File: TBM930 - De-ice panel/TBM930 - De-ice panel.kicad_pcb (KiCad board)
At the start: 2 copper layers, 190.5 x 101.6 mm, 51 parts, among them J1 SW_AIRFRAME_DE_ICE, J2 SW_ICE_LIGHT, J3 SW_PROP_DE_ICE, J4 SW_WIND_SHIELD, J5 SW_PITOT_L_HTR, J6 SW_PITOT_R_HTR, J7 SW_INERT_SEP, J8 Barrel_Jack, SW1 SW_Push, SW2 Mini toggle - SPDT, SW3 Mini toggle - SPDT, SW4 Mini toggle - SPDT, SW5 Mini toggle - SPDT, SW6 Mini toggle - SPDT, SW7 Mini toggle - SPDT, SW8 Mini toggle - SPDT, U1 Sparkfun_Pro_Micro, U2 TLC5917IN, U3 TLC5917IN

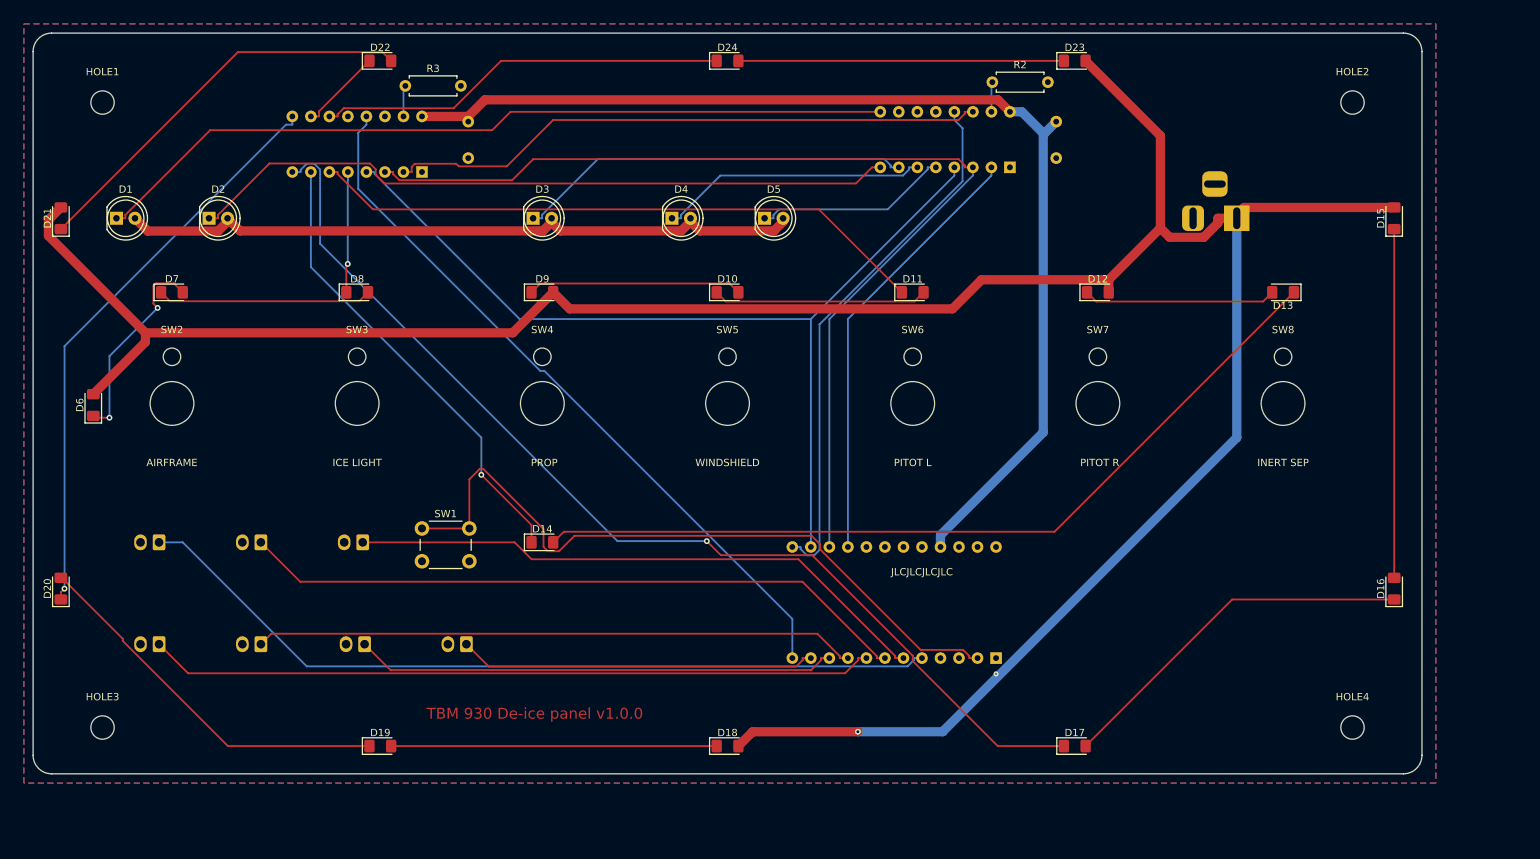
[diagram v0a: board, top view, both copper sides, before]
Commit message: Placed components on PCB, working on routing
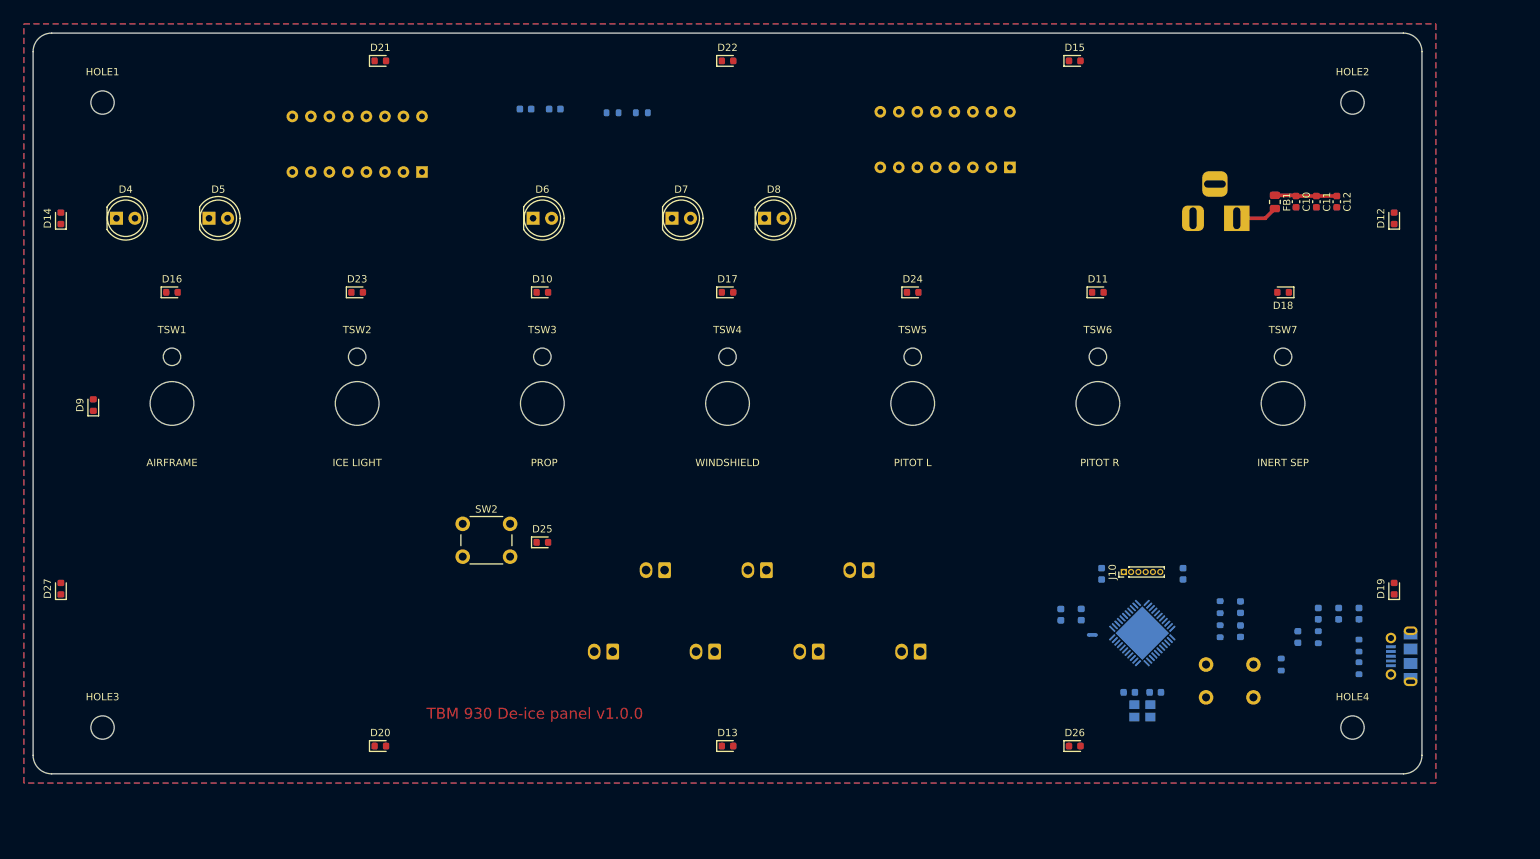
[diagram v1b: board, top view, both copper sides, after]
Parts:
- removed the J4 at (56.6, 126.4)
- removed the J5 at (70.6, 126.4)
- added C10: 10uF, Capacitor_SMD:C_0603_1608Metric, F.Cu at (212.6, 65.7)
- added C11: 1uF, Capacitor_SMD:C_0603_1608Metric, F.Cu at (215.4, 65.7)
- added C12: 0.1uF, Capacitor_SMD:C_0603_1608Metric, F.Cu at (218.2, 65.7)
- added C13: 0.1uF, Capacitor_SMD:C_0603_1608Metric, B.Cu at (106.9, 53.0)
- added C14: 0.1uF, Capacitor_SMD:C_0603_1608Metric, B.Cu at (110.9, 53.0)
- added C3: 20pF, Capacitor_SMD:C_0603_1608Metric, B.Cu at (189.7, 133.0)
- added C4: 20pF, Capacitor_SMD:C_0603_1608Metric, B.Cu at (193.3, 133.0)
- added C5: 10uF, Capacitor_SMD:C_0603_1608Metric, B.Cu at (221.2, 122.2)
- added C6: 1uF, Capacitor_SMD:C_0603_1608Metric, B.Cu at (218.4, 122.2)
- added C7: 0.1uF, Capacitor_SMD:C_0603_1608Metric, B.Cu at (215.6, 122.2)
- added C8: 1uF, Capacitor_SMD:C_0603_1608Metric, B.Cu at (183.1, 122.3)
- added C9: 0.1uF, Capacitor_SMD:C_0603_1608Metric, B.Cu at (180.3, 122.3)
- added D1: LED, LED_SMD:LED_0603_1608Metric, B.Cu at (212.9, 125.4)
- added D2: LED, LED_SMD:LED_0603_1608Metric, B.Cu at (205.0, 121.3)
- added D3: LED, LED_SMD:LED_0603_1608Metric, B.Cu at (205.0, 124.6)
- added FB1: Ferrite_Bead, Resistor_SMD:R_0805_2012Metric, F.Cu at (209.7, 65.7)
- added J1: USB_B_Micro, Connector_USB:USB_Micro-B_Molex-105017-0001, B.Cu at (227.1, 128.0)
- added J10: AVR-ISP-6, Connector_PinHeader_1.00mm:PinHeader_1x06_P1.00mm_Vertical, F.Cu at (189.0, 116.5)
- added J8: SW_PITOT_R_HTR, Connector_Molex:Molex_KK-254_AE-6410-02A_1x02_P2.54mm_Vertical, B.Cu at (147.1, 127.4)
- added J9: SW_INERT_SEP, Connector_Molex:Molex_KK-254_AE-6410-02A_1x02_P2.54mm_Vertical, B.Cu at (161.0, 127.4)
- added NT1: Net-Tie_2, NetTie:NetTie-2_SMD_Pad0.5mm, B.Cu at (184.7, 125.1)
- added R1: 10K, Resistor_SMD:R_0603_1608Metric, B.Cu at (210.6, 129.2)
- added R4: 1K, Resistor_SMD:R_0603_1608Metric, B.Cu at (215.6, 125.4)
- added R5: 330, Resistor_SMD:R_0603_1608Metric, B.Cu at (202.2, 121.3)
- added R6: 330, Resistor_SMD:R_0603_1608Metric, B.Cu at (202.2, 124.6)
- added R7: 1k, Resistor_SMD:R_0603_1608Metric, B.Cu at (118.9, 53.5)
- added R8: 1k, Resistor_SMD:R_0603_1608Metric, B.Cu at (122.9, 53.5)
- added SW2: SW_Push, Button_Switch_THT:SW_PUSH_6mm_H9.5mm, F.Cu at (98.3, 109.9)
- added Y1: 16MHz, Crystal:Crystal_SMD_3225-4Pin_3.2x2.5mm, B.Cu at (191.5, 135.5)
- C1, C2: value 0.1uF -> 1uF; footprint Capacitor_THT:C_Disc_D5.0mm_W2.5mm_P5.00mm -> Capacitor_SMD:C_0603_1608Metric
- D10: renamed from D9; footprint LED_SMD:LED_1206_3216Metric_Pad1.42x1.75mm_HandSolder -> LED_SMD:LED_0603_1608Metric
- D11: renamed from D12; footprint LED_SMD:LED_1206_3216Metric_Pad1.42x1.75mm_HandSolder -> LED_SMD:LED_0603_1608Metric
- D12: renamed from D15; footprint LED_SMD:LED_1206_3216Metric_Pad1.42x1.75mm_HandSolder -> LED_SMD:LED_0603_1608Metric
- D13: renamed from D18; footprint LED_SMD:LED_1206_3216Metric_Pad1.42x1.75mm_HandSolder -> LED_SMD:LED_0603_1608Metric
- D14: renamed from D21; footprint LED_SMD:LED_1206_3216Metric_Pad1.42x1.75mm_HandSolder -> LED_SMD:LED_0603_1608Metric
- D15: renamed from D23; footprint LED_SMD:LED_1206_3216Metric_Pad1.42x1.75mm_HandSolder -> LED_SMD:LED_0603_1608Metric
- D16: renamed from D7; footprint LED_SMD:LED_1206_3216Metric_Pad1.42x1.75mm_HandSolder -> LED_SMD:LED_0603_1608Metric
- D17: renamed from D10; footprint LED_SMD:LED_1206_3216Metric_Pad1.42x1.75mm_HandSolder -> LED_SMD:LED_0603_1608Metric
- D18: renamed from D13; footprint LED_SMD:LED_1206_3216Metric_Pad1.42x1.75mm_HandSolder -> LED_SMD:LED_0603_1608Metric
- D19: renamed from D16; footprint LED_SMD:LED_1206_3216Metric_Pad1.42x1.75mm_HandSolder -> LED_SMD:LED_0603_1608Metric
- D20: renamed from D19; footprint LED_SMD:LED_1206_3216Metric_Pad1.42x1.75mm_HandSolder -> LED_SMD:LED_0603_1608Metric
- D21: renamed from D22; footprint LED_SMD:LED_1206_3216Metric_Pad1.42x1.75mm_HandSolder -> LED_SMD:LED_0603_1608Metric
- D22: renamed from D24; footprint LED_SMD:LED_1206_3216Metric_Pad1.42x1.75mm_HandSolder -> LED_SMD:LED_0603_1608Metric
- D23: renamed from D8; footprint LED_SMD:LED_1206_3216Metric_Pad1.42x1.75mm_HandSolder -> LED_SMD:LED_0603_1608Metric
- D24: renamed from D11; footprint LED_SMD:LED_1206_3216Metric_Pad1.42x1.75mm_HandSolder -> LED_SMD:LED_0603_1608Metric
- D25: renamed from D14; footprint LED_SMD:LED_1206_3216Metric_Pad1.42x1.75mm_HandSolder -> LED_SMD:LED_0603_1608Metric
- D26: renamed from D17; footprint LED_SMD:LED_1206_3216Metric_Pad1.42x1.75mm_HandSolder -> LED_SMD:LED_0603_1608Metric
- D27: renamed from D20; footprint LED_SMD:LED_1206_3216Metric_Pad1.42x1.75mm_HandSolder -> LED_SMD:LED_0603_1608Metric
- D9: renamed from D6; footprint LED_SMD:LED_1206_3216Metric_Pad1.42x1.75mm_HandSolder -> LED_SMD:LED_0603_1608Metric
- J6: value SW_PITOT_R_HTR -> SW_WIND_SHIELD
- J7: value SW_INERT_SEP -> SW_PITOT_L_HTR
- R2, R3: value 1k -> 22; footprint Resistor_THT:R_Axial_DIN0207_L6.3mm_D2.5mm_P7.62mm_Horizontal -> Resistor_SMD:R_0603_1608Metric; moved to B.Cu
- SW1: footprint Button_Switch_THT:SW_PUSH_6mm_H9.5mm -> Button_Switch_THT:SW_PUSH_6mm_H4.3mm; moved to B.Cu
- U1: value Sparkfun_Pro_Micro -> ATmega16U4-MU-Exposed-Extra-Pins; footprint Arduino:Sparkfun_Pro_Micro -> Package_DFN_QFN:QFN-44-1EP_7x7mm_P0.5mm_EP5.2x5.2mm
- moved R3 151.7 mm to (221.2, 126.6), turned to 90 degrees
- moved SW1 115.6 mm to (206.8, 129.2), turned to 180 degrees
- moved C2 113.4 mm to (197.1, 116.7)
- moved R2 94.8 mm to (221.2, 129.7), turned to 270 degrees
- moved J4 69.4 mm to (140.0, 116.2)
- moved J5 69.4 mm to (153.9, 116.2)
- moved J3 69.4 mm to (126.0, 116.2)
- moved C1 57.4 mm to (185.9, 116.7)
- moved U1 49.4 mm to (191.5, 124.8), turned to 225 degrees
- moved J7 34.1 mm to (132.8, 127.4)
- moved J6 34.1 mm to (118.9, 127.4)
- renumbered D1 to D4, D2 to D5, D3 to D6, D4 to D7, D5 to D8, J8 to J2, J1 to J3, J2 to J4, J3 to J5, SW2 to TSW1, SW3 to TSW2, SW4 to TSW3, SW5 to TSW4, SW6 to TSW5, SW7 to TSW6, SW8 to TSW7
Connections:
- net Net-(U1-Pad1) renamed /D7
- net Net-(U1-Pad19) renamed /D2
- net Net-(U1-Pad20) renamed /RXI
- C1 pad 1: GND -> Net-(C1-Pad1)
- C1 pad 2: +5V -> GND
- C2 pad 1: GND -> Net-(C2-Pad1)
- C2 pad 2: +5V -> GND
- D4 pad 2: +5V_LED -> +5V
- D5 pad 2: +5V_LED -> +5V
- D6 pad 2: +5V_LED -> +5V
- D7 pad 2: +5V_LED -> +5V
- D8 pad 2: +5V_LED -> +5V
- J2 pad 1: +12V_LED -> /+12V
- J3 pad 1: AIRFRAME_DE_ICE -> SW_AIRFRAME
- J4 pad 1: ICE_LIGHT -> SW_ICE_LIGHT
- J5 pad 1: PROP_DE_ICE -> SW_PROP
- J6 pad 1: PITOT_R_HTR -> SW_WINDSHIELD
- J7 pad 1: INERT_SEP -> SW_PITOT_L
- R2 pad 1: Net-(R2-Pad1) -> Net-(J1-Pad3)
- R2 pad 2: GND -> /D+
- R3 pad 1: Net-(R3-Pad1) -> Net-(J1-Pad2)
- R3 pad 2: GND -> /D-
- SW1 pad 1: LTS_TEST -> /~RESET
- U1 pad 10: PITOT_R_HTR -> /MOSI
- U1 pad 11: INERT_SEP -> /MISO
- U1 pad 12: BACKLIGHT_BRIGHTNESS -> Net-(U1-Pad12)
- U1 pad 13: ANNUNCIATOR_BRIGHTNESS -> /~RESET
- U1 pad 14: LED_LATCH -> +5V
- U1 pad 15: LED_CLOCK -> GND
- U1 pad 16: LED_DATA -> /XTAL2
- U1 pad 17: Net-(U1-Pad17) -> /XTAL1
- U1 pad 18: Net-(U1-Pad18) -> INDICATOR_BRIGHT
- U1 pad 2: LTS_TEST -> +5V
- U1 pad 21: +5V -> /TXO
- U1 pad 24: Net-(U1-Pad24) -> +5V
- U1 pad 3: GND -> /D-
- U1 pad 4: GND -> /D+
- U1 pad 5: AIRFRAME_DE_ICE -> GND
- U1 pad 6: PROP_DE_ICE -> Net-(C2-Pad1)
- U1 pad 7: ICE_LIGHT -> +5V
- U1 pad 8: WIND_SHIELD -> /D17
- U1 pad 9: PITOT_L_HTR -> /SCK
- U2 pad 13: ANNUNCIATOR_BRIGHTNESS -> INDICATOR_BRIGHT
- U2 pad 15: Net-(R2-Pad1) -> Net-(R7-Pad1)
- U3 pad 13: BACKLIGHT_BRIGHTNESS -> BACKLIGHT_BRIGHT
- U3 pad 15: Net-(R3-Pad1) -> Net-(R8-Pad1)
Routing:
- net +12V_LED: track 361.9 -> 8.53 mm, vias 1 -> 0
- net +5V: track 153.8 -> 0.00 mm
- net BACKLIGHT4: track 145.9 -> 0.00 mm, vias 1 -> 0
- net LED_CLOCK: track 143.3 -> 0.00 mm
- net LED_LATCH: track 129.7 -> 0.00 mm
- net Net-(D18-Pad1): track 115.8 -> 0.00 mm
- net AIRFRAME_DE_ICE: track 112.3 -> 0.00 mm
- net AIRFRAME_1: track 111.1 -> 0.00 mm
- net BACKLIGHT_BRIGHTNESS: track 99.8 -> 0.00 mm
- net WIND_SHIELD: track 99.7 -> 0.00 mm
- net LTS_TEST: track 98.0 -> 0.00 mm
- net AIRFRAME_2: track 97.9 -> 0.00 mm
- net +5V_LED: track 95.2 -> 0.00 mm
- net ICE_LIGHT: track 92.3 -> 0.00 mm
- net BACKLIGHT2: track 85.5 -> 0.00 mm
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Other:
- net class +12V_LED removed
- net class +5V removed
- net class +5V_LED removed
- net class GND removed
- net class POWER added: clearance 0.2, trace_width 0.508, via_dia 0.8, via_drill 0.4
- board text removed: "JLCJLCJLCJLC"

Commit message: More atmega32u4 routing
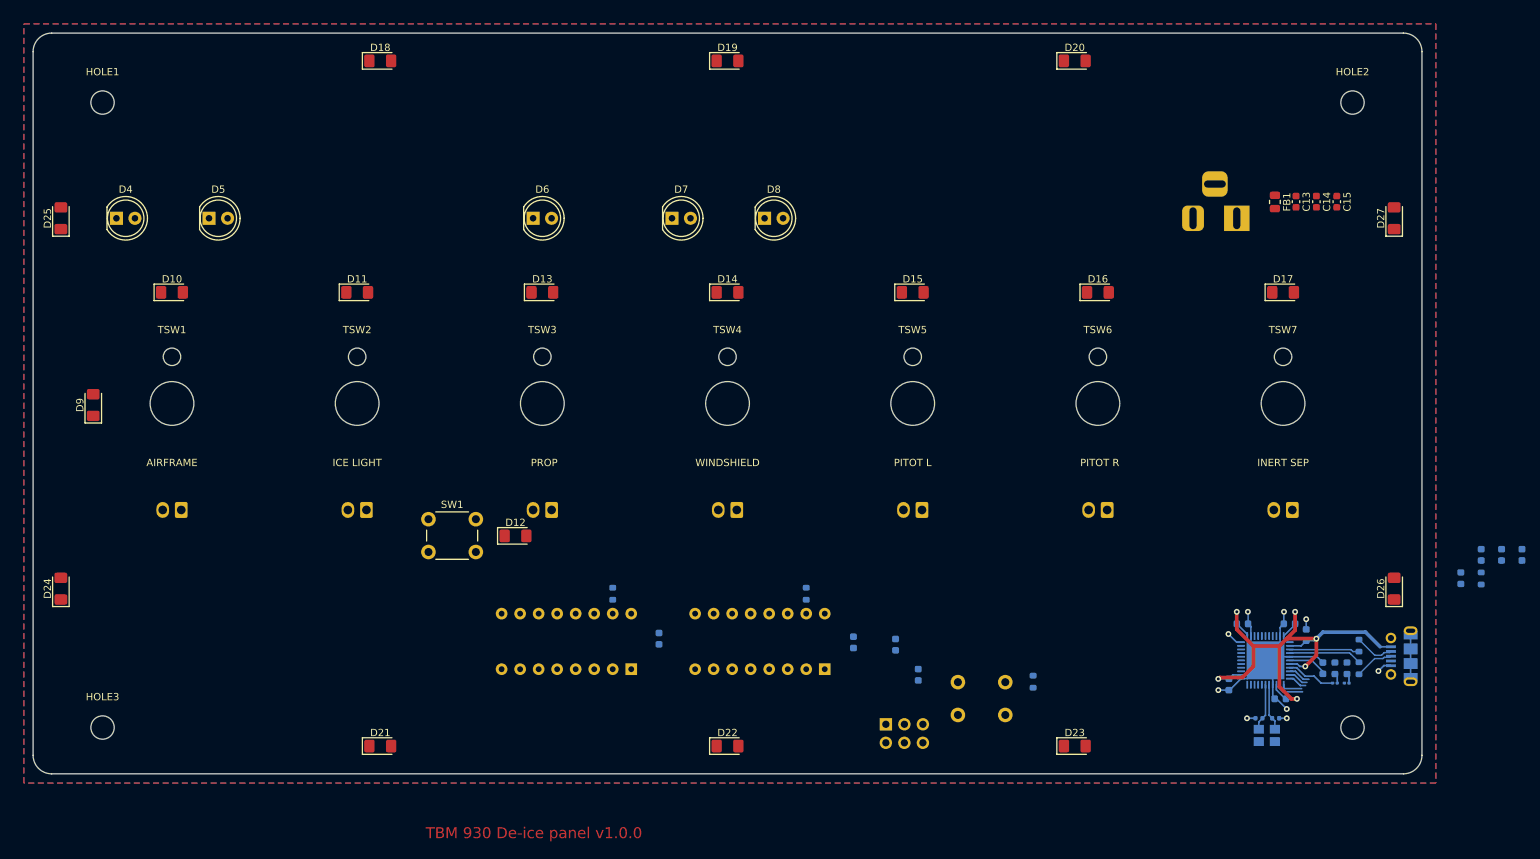
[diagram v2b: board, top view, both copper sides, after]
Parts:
- removed the C13 at (106.9, 53.0)
- removed the J3 at (126.0, 116.2)
- removed NT1: Net-Tie_2, NetTie:NetTie-2_SMD_Pad0.5mm
- removed the R6 at (202.2, 124.6)
- removed the R7 at (118.9, 53.5)
- removed the R8 at (122.9, 53.5)
- removed the SW1 at (206.8, 129.2)
- removed the U1 at (191.5, 124.8)
- added C1: 10uF, Capacitor_SMD:C_0603_1608Metric, B.Cu at (214.0, 125.1)
- added C16: 20pF, Capacitor_SMD:C_0402_1005Metric, B.Cu at (207.5, 136.5)
- added C17: 20pF, Capacitor_SMD:C_0402_1005Metric, B.Cu at (209.8, 136.5)
- added C7: 1uF, Capacitor_SMD:C_0603_1608Metric, B.Cu at (216.3, 129.7)
- added C8: 0.1uF, Capacitor_SMD:C_0603_1608Metric, B.Cu at (125.2, 125.6)
- added J1: SW_AIRFRAME_DE_ICE, Connector_Molex:Molex_KK-254_AE-6410-02A_1x02_P2.54mm_Vertical, B.Cu at (59.7, 108.0)
- added R2: 330, Resistor_SMD:R_0201_0603Metric, B.Cu at (217.9, 131.7)
- added R3: 1k, Resistor_SMD:R_0603_1608Metric, B.Cu at (145.4, 119.4)
- added R4: 1k, Resistor_SMD:R_0603_1608Metric, B.Cu at (118.9, 119.4)
- added SW2: SW_Push, Button_Switch_THT:SW_PUSH_6mm_H4.3mm, B.Cu at (172.7, 131.6)
- added U2: TLC5917IN, Package_DIP:DIP-16_W7.62mm, B.Cu at (121.4, 129.8)
- C2: value 1uF -> 0.1uF
- C3, C4: value 20pF -> 0.1uF
- D1: renamed from D2; value LED -> YELLOW
- D10, D11, D12, D13, D14, D15, D16, D17, D18, D19, D20, D21, D22, D23, D24, D25, D26, D27, D9: footprint LED_SMD:LED_0603_1608Metric -> LED_SMD:LED_1206_3216Metric_Pad1.42x1.75mm_HandSolder
- D2: renamed from D3; value LED -> GREEN
- D3: renamed from D1; value LED -> GREEN
- J10: footprint Connector_PinHeader_1.00mm:PinHeader_1x06_P1.00mm_Vertical -> Connector_PinHeader_2.54mm:PinHeader_2x03_P2.54mm_Vertical; moved to B.Cu
- R5: footprint Resistor_SMD:R_0603_1608Metric -> Resistor_SMD:R_0201_0603Metric
- U3: value TLC5917IN -> ATmega32U4-MU; footprint Package_DIP:DIP-16_W7.62mm -> Package_DFN_QFN:QFN-44-1EP_7x7mm_P0.5mm_EP5.2x5.2mm
- moved D27 189.8 mm to (226.1, 67.9)
- moved D20 133.8 mm to (182.2, 46.4)
- moved U3 133.7 mm to (208.4, 128.6), turned to 180 degrees
- moved D12 128.2 mm to (105.5, 111.5), turned to 0 degrees
- moved D18 127.8 mm to (87.0, 46.4), turned to 0 degrees
- moved D16 127.0 mm to (185.4, 78.1)
- moved D24 123.7 mm to (43.2, 118.7), turned to 90 degrees
- moved D19 116.6 mm to (134.6, 46.4), turned to 0 degrees
- moved D23 116.4 mm to (182.2, 140.3)
- moved D11 101.6 mm to (83.8, 78.1)
- moved D21 94.0 mm to (87.0, 140.3)
- moved D22 94.0 mm to (134.6, 140.3)
- moved D14 92.0 mm to (134.6, 78.1), turned to 0 degrees
- moved C9 83.8 mm to (151.9, 126.1), turned to 90 degrees
- moved D25 79.6 mm to (43.2, 67.9), turned to 90 degrees
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- renumbered C8 to C1, C5 to C10, C6 to C11, C7 to C12, C10 to C13, C11 to C14, C12 to C15, C9 to C5, C1 to C6, C14 to C9, J4 to J2, J5 to J3, J6 to J4, J7 to J5, J8 to J6, J9 to J7, J2 to J8, J1 to J9, R4 to R6, R2 to R7, R3 to R8, SW2 to SW1, U2 to U1
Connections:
- net Net-(J1-Pad2) renamed /DR-
- net Net-(J1-Pad3) renamed /DR+
- C2 pad 1: Net-(C2-Pad1) -> +5V
- C3 pad 1: /XTAL1 -> +5V
- C4 pad 1: /XTAL2 -> +5V
- C6 pad 1: Net-(C1-Pad1) -> Net-(C6-Pad1)
- D1 pad 2: Net-(D2-Pad2) -> Net-(D1-Pad2)
- D10 pad 2: +12V_LED -> Net-(D10-Pad2)
- D11 pad 1: Net-(D11-Pad1) -> BACKLIGHT1
- D11 pad 2: +12V_LED -> Net-(D10-Pad1)
- D13 pad 2: +12V_LED -> Net-(D12-Pad1)
- D14 pad 1: Net-(D14-Pad1) -> BACKLIGHT2
- D14 pad 2: +12V_LED -> Net-(D13-Pad1)
- D16 pad 2: Net-(D16-Pad2) -> Net-(D15-Pad1)
- D17 pad 1: Net-(D17-Pad1) -> BACKLIGHT3
- D17 pad 2: Net-(D10-Pad1) -> Net-(D16-Pad1)
- D18 pad 2: Net-(D11-Pad1) -> +12V_LED
- D19 pad 2: Net-(D12-Pad1) -> Net-(D18-Pad1)
- D2 pad 2: Net-(D3-Pad2) (its old number) -> Net-(D2-Pad2)
- D20 pad 1: Net-(D20-Pad1) -> BACKLIGHT4
- D20 pad 2: Net-(D13-Pad1) -> Net-(D19-Pad1)
- D21 pad 1: BACKLIGHT6 -> Net-(D21-Pad1)
- D21 pad 2: Net-(D14-Pad1) -> +12V_LED
- D22 pad 1: BACKLIGHT7 -> Net-(D22-Pad1)
- D22 pad 2: Net-(D15-Pad1) -> Net-(D21-Pad1)
- D23 pad 1: BACKLIGHT1 -> BACKLIGHT5
- D23 pad 2: Net-(D16-Pad1) -> Net-(D22-Pad1)
- D24 pad 1: BACKLIGHT2 -> Net-(D24-Pad1)
- D24 pad 2: Net-(D17-Pad1) -> +12V_LED
- D25 pad 1: BACKLIGHT3 -> BACKLIGHT6
- D25 pad 2: Net-(D18-Pad1) -> Net-(D24-Pad1)
- D26 pad 1: BACKLIGHT4 -> Net-(D26-Pad1)
- D26 pad 2: Net-(D19-Pad1) -> +12V_LED
- D27 pad 1: BACKLIGHT5 -> BACKLIGHT7
- D27 pad 2: Net-(D20-Pad1) -> Net-(D26-Pad1)
- D9 pad 1: Net-(D16-Pad2) -> Net-(D10-Pad2)
- R5 pad 1: /D17 -> Net-(D2-Pad2)
- R5 pad 2: Net-(D2-Pad2) -> Net-(R5-Pad2)
- U1 pad 14: Net-(U2-Pad14) -> Net-(U1-Pad14)
- U3 pad 1: GND -> /D7
- U3 pad 10: BACKLIGHT6 -> /MOSI
- U3 pad 11: BACKLIGHT7 -> /MISO
- U3 pad 12: Net-(U3-Pad12) -> SW_LTS_TEST
- U3 pad 13: BACKLIGHT_BRIGHT -> /~RESET
- U3 pad 14: Net-(U3-Pad14) -> +5V
- U3 pad 15: Net-(R8-Pad1) -> GND
- U3 pad 16: +5V -> /XTAL2
- U3 pad 2: Net-(U2-Pad14) -> +5V
- U3 pad 3: LED_CLOCK -> /D-
- U3 pad 4: LED_LATCH -> /D+
- U3 pad 5: BACKLIGHT1 -> GND
- U3 pad 6: BACKLIGHT2 -> Net-(C7-Pad1)
- U3 pad 7: BACKLIGHT3 -> +5V
- U3 pad 8: BACKLIGHT4 -> /D17
- U3 pad 9: BACKLIGHT5 -> /SCK
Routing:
- net +5V: track 0.00 -> 73.3 mm, vias 0 -> 6
- net GND: track 0.00 -> 53.6 mm, vias 0 -> 9
- net /D+: track 0.00 -> 10.0 mm
- net /D-: track 0.00 -> 9.61 mm
- net +12V_LED: track 8.53 -> 0.00 mm
- net /D17: track 0.00 -> 6.74 mm
- net /XTAL1: track 0.00 -> 6.48 mm
- net /XTAL2: track 0.00 -> 6.43 mm
- net /+12V: track 5.78 -> 0.00 mm
- net /DR-: track 0.00 -> 5.49 mm
- net Net-(C7-Pad1): track 0.00 -> 5.48 mm
- net /DR+: track 0.00 -> 5.41 mm
- net /~RESET: track 0.00 -> 3.83 mm
- net /SCK: track 0.00 -> 3.07 mm
- net SW_LTS_TEST: track 0.00 -> 2.97 mm
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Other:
- net class 12V added: clearance 0.2, trace_width 0.508, via_dia 0.8, via_drill 0.4
- net class Default: trace_width 0.25 -> 0.2286
- net class POWER: trace_width 0.508 -> 0.2286
- board text removed: "GND"
